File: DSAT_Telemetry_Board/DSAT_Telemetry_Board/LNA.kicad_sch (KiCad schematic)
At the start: 1 part

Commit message: added Beck edits
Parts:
- removed U?: PSA4-5043+, Package_TO_SOT_SMD:SOT-343_SC-70-4_Handsoldering, symbol DSAT_Telemetry_Libraries:PSA4-5043+
- added C?: 0.1uF, symbol Device:C
- added C?: 100pF, symbol Device:C
- added C?: 1.5nF, symbol Device:C
- added L?: 3uH, symbol Device:L
- added U?: PSA4-5043+, Package_TO_SOT_SMD:SOT-343_SC-70-4_Handsoldering, symbol DSAT_Telemetry_Libraries:PSA4-5043+
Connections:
- new net: C?.1, L?.2, U?.1 (RFout)
- new net: C?.2, U?.3 (RFin)
- new net +3.3V: C?.1, L?.1
- new net GND: C?.2, U?.2 (Gnd), U?.4 (Gnd)
- new net TX_Duplexer: C?.2
- new net TX_Transciever: C?.1
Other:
- note added: "Bias Tee"
- note added: "Data Sheets says 3V or 5V, unsure if +3.3V will work or not, but worth trying"
- note added: "Input High Pass Capacitor"
- note added: "Power Filter"
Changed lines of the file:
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@@
 (kicad_sch (version 20211123) (generator eeschema)
   (paper "A4")
-  (symbol (lib_id "DSAT_Telemetry_Libraries:PSA4-5043+") (at 133.35 83.82 0) (unit 1)
+  (junction (at 140.97 124.46) (diameter 0) (color 0 0 0 0)
+  )
+  (junction (at 161.29 104.14) (diameter 0) (color 0 0 0 0)
+  )
+  (junction (at 184.15 82.55) (diameter 0) (color 0 0 0 0)
+  )
+  (wire (pts (xy 161.29 82.55) (xy 161.29 90.17))
+    (stroke (width 0) (type default) (color 0 0 0 0))
+  )
+  (wire (pts (xy 154.94 110.49) (xy 149.86 110.49))
+    (stroke (width 0) (type default) (color 0 0 0 0))
+  )
+  (wire (pts (xy 132.08 110.49) (xy 127 110.49))
+    (stroke (width 0) (type default) (color 0 0 0 0))
+  )
+  (wire (pts (xy 161.29 82.55) (xy 184.15 82.55))
+    (stroke (width 0) (type default) (color 0 0 0 0))
+  )
+  (wire (pts (xy 154.94 110.49) (xy 154.94 124.46))
+    (stroke (width 0) (type default) (color 0 0 0 0))
+  )
+  (wire (pts (xy 124.46 104.14) (xy 132.08 104.14))
+    (stroke (width 0) (type default) (color 0 0 0 0))
+  )
+  (wire (pts (xy 109.22 104.14) (xy 116.84 104.14))
+    (stroke (width 0) (type default) (color 0 0 0 0))
+  )
+  (wire (pts (xy 154.94 124.46) (xy 140.97 124.46))
+    (stroke (width 0) (type default) (color 0 0 0 0))
+  )
+  (wire (pts (xy 149.86 104.14) (xy 161.29 104.14))
+    (stroke (width 0) (type default) (color 0 0 0 0))
+  )
+  (wire (pts (xy 161.29 104.14) (xy 170.18 104.14))
+    (stroke (width 0) (type default) (color 0 0 0 0))
+  )
+  (wire (pts (xy 184.15 78.74) (xy 184.15 82.55))
+    (stroke (width 0) (type default) (color 0 0 0 0))
+  )
+  (wire (pts (xy 177.8 104.14) (xy 193.04 104.14))
+    (stroke (width 0) (type default) (color 0 0 0 0))
+  )
+  (wire (pts (xy 161.29 97.79) (xy 161.29 104.14))
+    (stroke (width 0) (type default) (color 0 0 0 0))
+  )
+  (wire (pts (xy 127 110.49) (xy 127 124.46))
+    (stroke (width 0) (type default) (color 0 0 0 0))
+  )
+  (wire (pts (xy 127 124.46) (xy 140.97 124.46))
+    (stroke (width 0) (type default) (color 0 0 0 0))
+  )
+  (text "Power Filter\n" (at 194.31 85.09 0)
+    (effects (font (size 1.27 1.27)) (justify left bottom))
+  )
+  (text "Bias Tee\n" (at 160.02 107.95 0)
+    (effects (font (size 1.27 1.27)) (justify left bottom))
+  )
+  (text "Input High Pass Capacitor\n" (at 109.22 93.98 0)
+    (effects (font (size 1.27 1.27)) (justify left bottom))
+  )
+  (text "Data Sheets says 3V or 5V, unsure if +3.3V will work or not, but worth trying\n"
+    (at 148.59 71.12 0)
+    (effects (font (size 1.27 1.27)) (justify left bottom))
+  )
+  (hierarchical_label "TX_Transciever" (shape input) (at 109.22 104.14 180)
+    (effects (font (size 1.27 1.27)) (justify right))
+  )
+  (hierarchical_label "TX_Duplexer" (shape input) (at 193.04 104.14 0)
+    (effects (font (size 1.27 1.27)) (justify left))
+  )
+  (symbol (lib_id "DSAT_Telemetry_Libraries:PSA4-5043+") (at 140.97 96.52 0) (unit 1)
     (in_bom yes) (on_board yes) (fields_autoplaced)
-    (property "Reference" "U?" (id 0) (at 133.35 83.82 0))
-    (property "Value" "PSA4-5043+" (id 1) (at 133.35 86.36 0))
-    (property "Footprint" "Package_TO_SOT_SMD:SOT-343_SC-70-4_Handsoldering" (id 2) (at 134.62 104.14 0)
+    (property "Reference" "U?" (id 0) (at 140.97 96.52 0))
+    (property "Value" "PSA4-5043+" (id 1) (at 140.97 99.06 0))
+    (property "Footprint" "Package_TO_SOT_SMD:SOT-343_SC-70-4_Handsoldering" (id 2) (at 142.24 116.84 0)
       (effects (font (size 1.27 1.27)) hide)
     )
-    (property "Datasheet" "" (id 3) (at 133.35 83.82 0)
+    (property "Datasheet" "" (id 3) (at 140.97 96.52 0)
       (effects (font (size 1.27 1.27)) hide)
     )
@@
     (pin "4")
   )
+  (symbol (lib_id "power:GND") (at 140.97 124.46 0) (unit 1)
+    (in_bom yes) (on_board yes) (fields_autoplaced)
+    (property "Reference" "#PWR?" (id 0) (at 140.97 130.81 0)
+      (effects (font (size 1.27 1.27)) hide)
+    )
+    (property "Value" "GND" (id 1) (at 140.97 129.54 0))
+    (property "Footprint" "" (id 2) (at 140.97 124.46 0)
+      (effects (font (size 1.27 1.27)) hide)
+    )
+    (property "Datasheet" "" (id 3) (at 140.97 124.46 0)
+      (effects (font (size 1.27 1.27)) hide)
+    )
+    (pin "1")
+  )
+  (symbol (lib_id "Device:L") (at 161.29 93.98 0) (unit 1)
+    (in_bom yes) (on_board yes) (fields_autoplaced)
+    (property "Reference" "L?" (id 0) (at 162.56 92.7099 0)
+      (effects (font (size 1.27 1.27)) (justify left))
+    )
+    (property "Value" "3uH" (id 1) (at 162.56 95.2499 0)
+      (effects (font (size 1.27 1.27)) (justify left))
+    )
+    (property "Footprint" "" (id 2) (at 161.29 93.98 0)
+      (effects (font (size 1.27 1.27)) hide)
+    )
+    (property "Datasheet" "~" (id 3) (at 161.29 93.98 0)
+      (effects (font (size 1.27 1.27)) hide)
+    )
+    (pin "1")
+    (pin "2")
+  )
+  (symbol (lib_id "power:+3.3V") (at 184.15 78.74 0) (unit 1)
+    (in_bom yes) (on_board yes) (fields_autoplaced)
+    (property "Reference" "#PWR?" (id 0) (at 184.15 82.55 0)
+      (effects (font (size 1.27 1.27)) hide)
+    )
+    (property "Value" "+3.3V" (id 1) (at 184.15 73.66 0))
+    (property "Footprint" "" (id 2) (at 184.15 78.74 0)
+      (effects (font (size 1.27 1.27)) hide)
+    )
+    (property "Datasheet" "" (id 3) (at 184.15 78.74 0)
+      (effects (font (size 1.27 1.27)) hide)
+    )
+    (pin "1")
+  )
+  (symbol (lib_id "Device:C") (at 184.15 86.36 0) (unit 1)
+    (in_bom yes) (on_board yes) (fields_autoplaced)
+    (property "Reference" "C?" (id 0) (at 187.96 85.0899 0)
+      (effects (font (size 1.27 1.27)) (justify left))
+    )
+    (property "Value" "0.1uF" (id 1) (at 187.96 87.6299 0)
+      (effects (font (size 1.27 1.27)) (justify left))
+    )
+    (property "Footprint" "" (id 2) (at 185.1152 90.17 0)
+      (effects (font (size 1.27 1.27)) hide)
+    )
+    (property "Datasheet" "~" (id 3) (at 184.15 86.36 0)
+      (effects (font (size 1.27 1.27)) hide)
+    )
+    (pin "1")
+    (pin "2")
+  )
+  (symbol (lib_id "Device:C") (at 120.65 104.14 90) (mirror x) (unit 1)
+    (in_bom yes) (on_board yes) (fields_autoplaced)
+    (property "Reference" "C?" (id 0) (at 120.65 96.52 90))
+    (property "Value" "100pF" (id 1) (at 120.65 99.06 90))
+    (property "Footprint" "" (id 2) (at 124.46 105.1052 0)
+      (effects (font (size 1.27 1.27)) hide)
+    )
+    (property "Datasheet" "~" (id 3) (at 120.65 104.14 0)
+      (effects (font (size 1.27 1.27)) hide)
+    )
+    (pin "1")
+    (pin "2")
+  )
+  (symbol (lib_id "power:GND") (at 184.15 90.17 0) (unit 1)
+    (in_bom yes) (on_board yes) (fields_autoplaced)
+    (property "Reference" "#PWR?" (id 0) (at 184.15 96.52 0)
+      (effects (font (size 1.27 1.27)) hide)
+    )
+    (property "Value" "GND" (id 1) (at 184.15 95.25 0))
+    (property "Footprint" "" (id 2) (at 184.15 90.17 0)
+      (effects (font (size 1.27 1.27)) hide)
+    )
+    (property "Datasheet" "" (id 3) (at 184.15 90.17 0)
+      (effects (font (size 1.27 1.27)) hide)
+    )
+    (pin "1")
+  )
+  (symbol (lib_id "Device:C") (at 173.99 104.14 90) (mirror x) (unit 1)
+    (in_bom yes) (on_board yes) (fields_autoplaced)
+    (property "Reference" "C?" (id 0) (at 173.99 96.52 90))
+    (property "Value" "1.5nF" (id 1) (at 173.99 99.06 90))
+    (property "Footprint" "" (id 2) (at 177.8 105.1052 0)
+      (effects (font (size 1.27 1.27)) hide)
+    )
+    (property "Datasheet" "~" (id 3) (at 173.99 104.14 0)
+      (effects (font (size 1.27 1.27)) hide)
+    )
+    (pin "1")
+    (pin "2")
+  )
 )

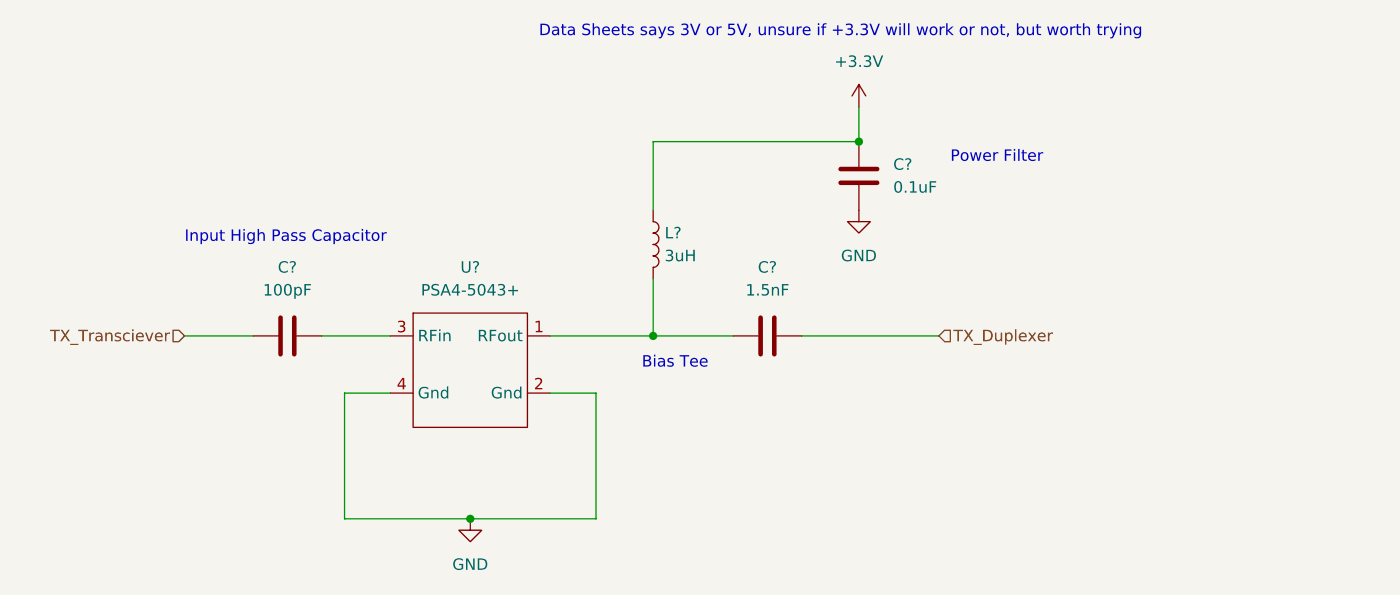
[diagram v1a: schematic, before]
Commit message: Added Watchdog Timer
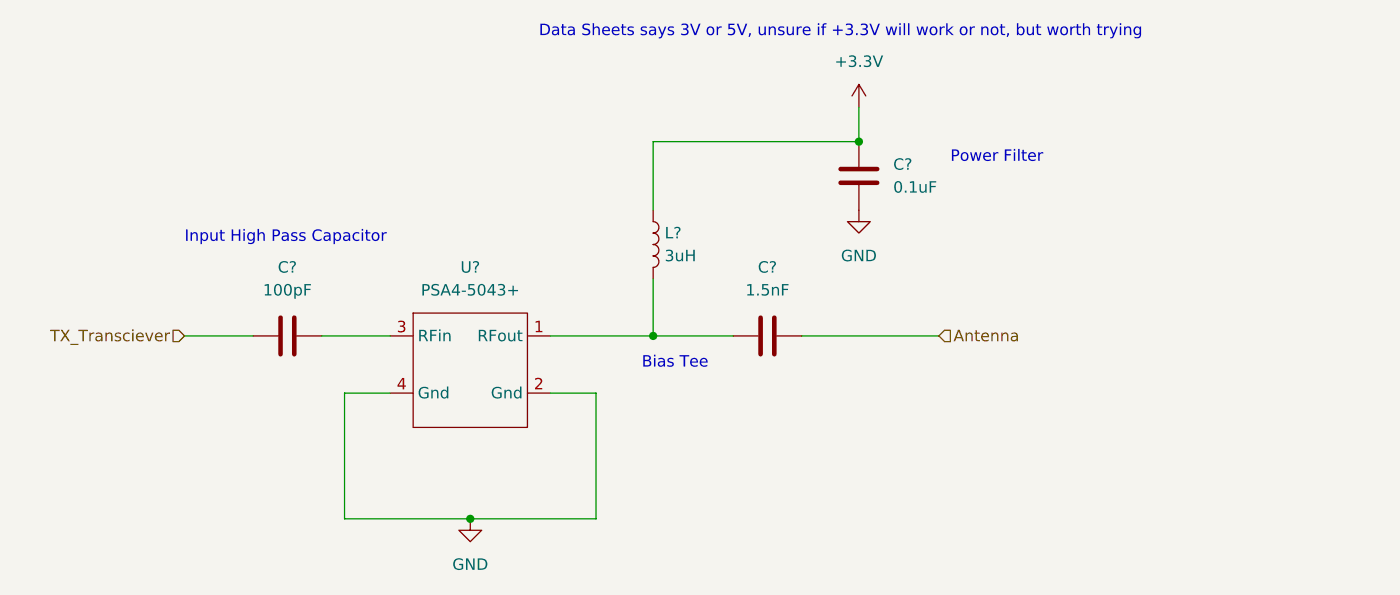
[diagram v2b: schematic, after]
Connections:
- net TX_Duplexer renamed Antenna
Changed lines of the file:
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@@
     (effects (font (size 1.27 1.27)) (justify right))
   )
-  (hierarchical_label "TX_Duplexer" (shape input) (at 193.04 104.14 0)
+  (hierarchical_label "Antenna" (shape input) (at 193.04 104.14 0)
     (effects (font (size 1.27 1.27)) (justify left))
   )

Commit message: Added Transciever Updates/Biases/RF_Switch
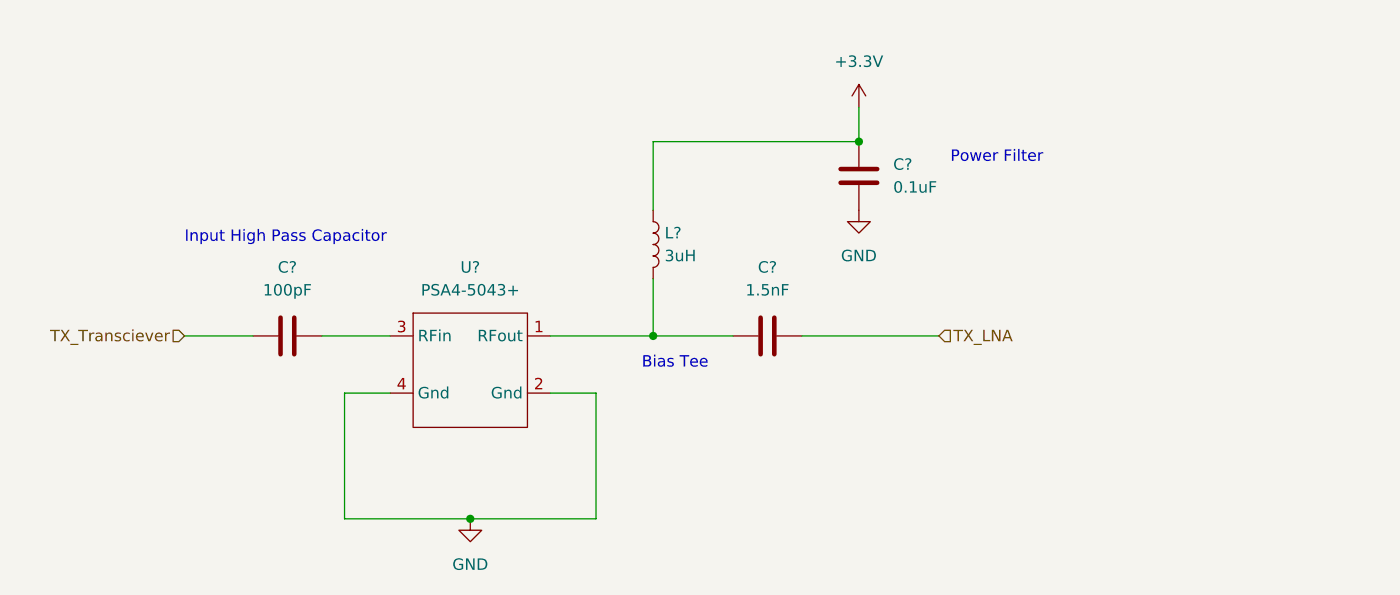
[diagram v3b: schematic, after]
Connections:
- net Antenna renamed TX_LNA
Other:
- note removed: "Data Sheets says 3V or 5V, unsure if +3.3V will work or not, but worth trying"
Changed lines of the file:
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@@
-    (effects (font (size 1.27 1.27)) (justify left bottom))
-  )
-  (text "Data Sheets says 3V or 5V, unsure if +3.3V will work or not, but worth trying\n"
-    (at 148.59 71.12 0)
     (effects (font (size 1.27 1.27)) (justify left bottom))
   )
@@
     (effects (font (size 1.27 1.27)) (justify right))
   )
-  (hierarchical_label "Antenna" (shape input) (at 193.04 104.14 0)
+  (hierarchical_label "TX_LNA" (shape input) (at 193.04 104.14 0)
     (effects (font (size 1.27 1.27)) (justify left))
   )

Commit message: Added Matching Networks/Linear Regulator/Watchdog Pins
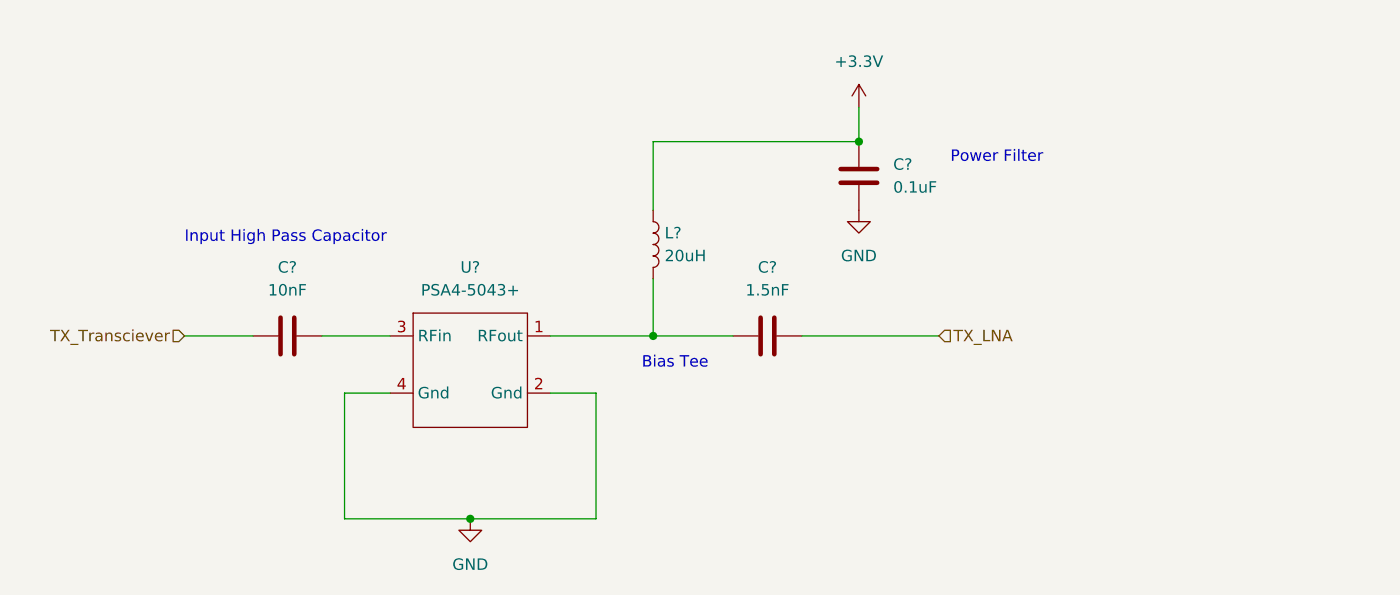
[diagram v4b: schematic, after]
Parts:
- C?: value 100pF -> 10nF
- L?: value 3uH -> 20uH
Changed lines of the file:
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@@
       (effects (font (size 1.27 1.27)) (justify left))
     )
-    (property "Value" "3uH" (id 1) (at 162.56 95.2499 0)
+    (property "Value" "20uH" (id 1) (at 162.56 95.2499 0)
       (effects (font (size 1.27 1.27)) (justify left))
     )
@@
     (in_bom yes) (on_board yes) (fields_autoplaced)
     (property "Reference" "C?" (id 0) (at 120.65 96.52 90))
-    (property "Value" "100pF" (id 1) (at 120.65 99.06 90))
+    (property "Value" "10nF" (id 1) (at 120.65 99.06 90))
     (property "Footprint" "" (id 2) (at 124.46 105.1052 0)
       (effects (font (size 1.27 1.27)) hide)
